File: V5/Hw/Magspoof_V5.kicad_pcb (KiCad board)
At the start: 2 copper layers, 76.5 x 32.5 mm, 59 parts, among them J1 SWD, J2 SWD, P1 USB_C_Plug_USB2.0, Q1 DMG3415U-7, SW1 ON, SW3 S1, SW4 SOURCE MAG, SW5 RESET, U1 CH552G, U2 AP2112K-3.3, U3 TC4424, U5 MCP73831

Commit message: feat(hw): logos
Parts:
- moved kibuzzard-6435F3C4 4.80 mm to (145.2, 50.0)
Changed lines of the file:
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@@
 	(footprint "kibuzzard-6435F3C4"
 		(layer "F.Cu")
-		(at 140.42 50.31 90)
+		(at 145.21 50.01 90)
 		(descr "Generated with KiBuzzard")
 		(tags "kb_params=eyJBbGlnbm1lbnRDaG9pY2UiOiAiQ2VudGVyIiwgIkNhcExlZnRDaG9pY2UiOiAiWyIsICJDYXBSaWdodENob2ljZSI6ICJdIiwgIkZvbnRDb21ib0JveCI6ICJVYnVudHVNb25vLUIiLCAiSGVpZ2h0Q3RybCI6ICIuOCIsICJMYXllckNvbWJvQm94IjogIkYuU2lsa1MiLCAiTXVsdGlMaW5lVGV4dCI6ICJDT0lMIiwgIlBhZGRpbmdCb3R0b21DdHJsIjogIjUiLCAiUGFkZGluZ0xlZnRDdHJsIjogIjUiLCAiUGFkZGluZ1JpZ2h0Q3RybCI6ICI1IiwgIlBhZGRpbmdUb3BDdHJsIjogIjUiLCAiV2lkdGhDdHJsIjogIiJ9")
@@
 		(tags "Through hole pin header THT 1x04 2.54mm single row")
 		(property "Reference" "J2"
-			(at 0 -2.33 270)
+			(at 0 -2.33 -90)
 			(layer "F.SilkS")
 			(effects
@@
 		)
 		(property "Value" "SWD"
-			(at 0 9.95 270)
+			(at 0 9.95 -90)
 			(layer "F.Fab")
 			(effects
@@
 		)
 		(fp_text user "${REFERENCE}"
-			(at 0 3.81 360)
+			(at 0 3.81 0)
 			(layer "F.Fab")
 			(effects

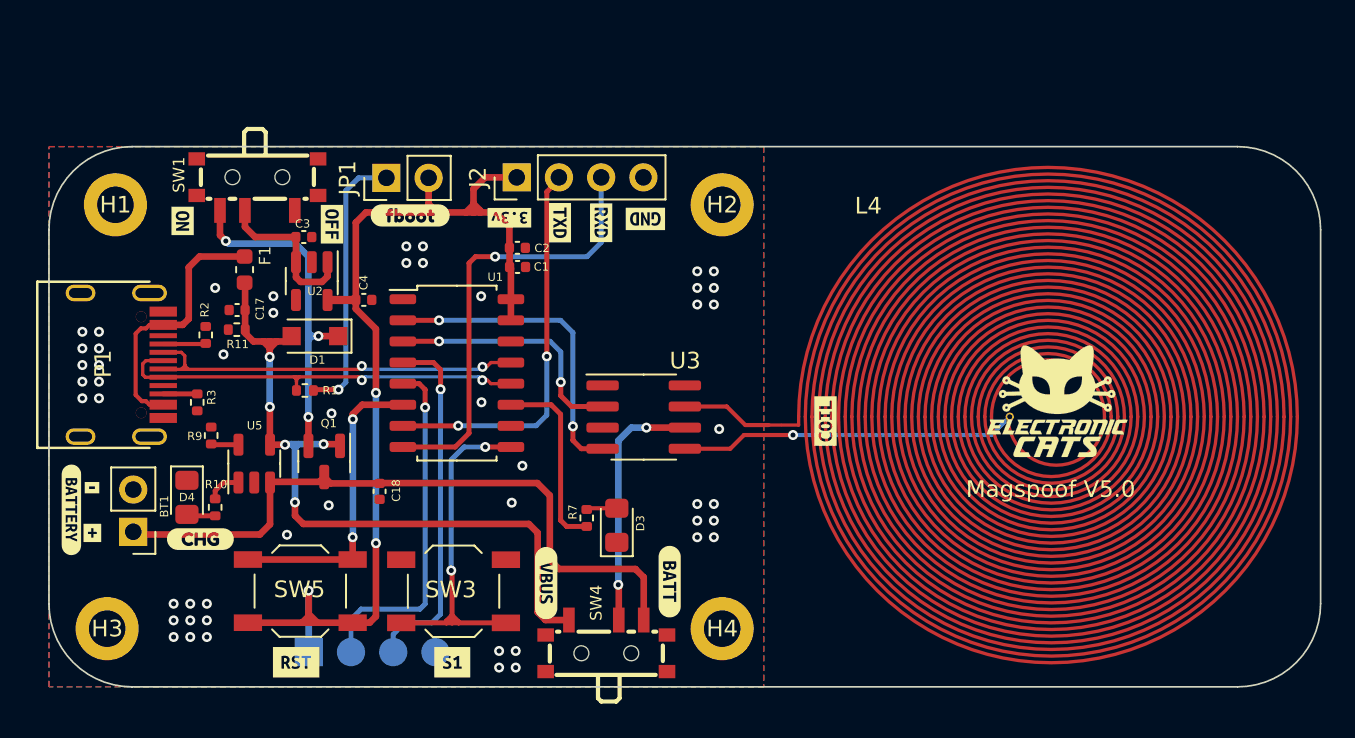
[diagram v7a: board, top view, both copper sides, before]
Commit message: feat(hw): components organization updated
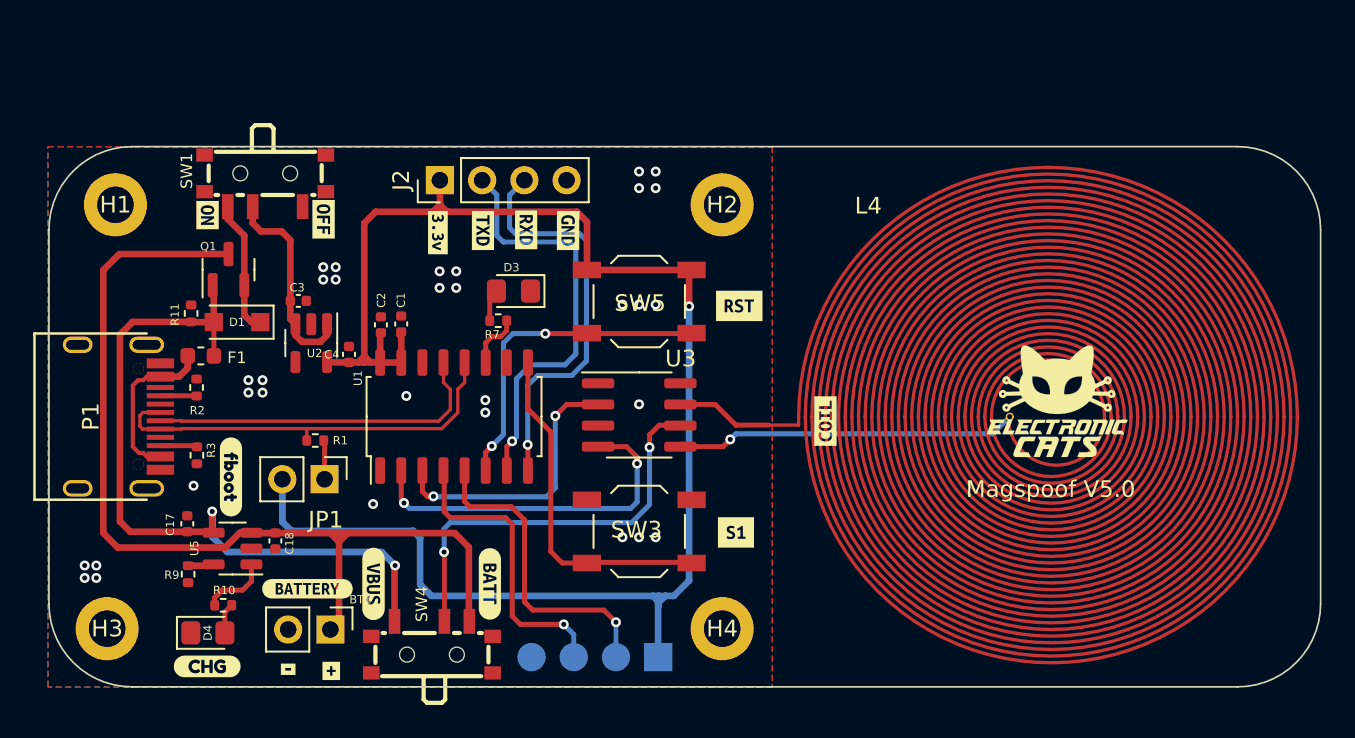
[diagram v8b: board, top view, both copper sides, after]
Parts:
- moved kibuzzard-660F1CC0 34.2 mm to (140.0, 43.1)
- moved SW5 26.8 mm to (134.0, 42.8), turned to 180 degrees
- moved kibuzzard-6616D983 22.1 mm to (135.2, 60.1)
- moved J1 21.0 mm to (135.2, 64.2), turned to 90 degrees
- moved kibuzzard-64665C9F 19.1 mm to (109.5, 53.4), turned to -90 degrees
- moved kibuzzard-660F1CCE 18.8 mm to (139.8, 56.7)
- moved JP1 18.5 mm to (115.1, 53.5), turned to -90 degrees
- moved kibuzzard-6436EA37 16.6 mm to (115.5, 65.0)
- moved kibuzzard-6616D9B1 16.2 mm to (132.6, 59.4)
- moved kibuzzard-6436EA46 16.1 mm to (112.9, 64.9)
- moved D3 15.4 mm to (126.4, 42.2), turned to 180 degrees
- moved kibuzzard-6616DCE6 15.0 mm to (114.0, 60.1), turned to 0 degrees
- moved BT1 13.2 mm to (115.4, 62.5), turned to -90 degrees
- moved C17 13.2 mm to (106.8, 56.2), turned to 90 degrees
- moved R7 13.0 mm to (125.5, 44.0), turned to 180 degrees
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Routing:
- net +3V3: track 65.8 -> 98.8 mm, vias 3 -> 1
- net +BATT: track 41.0 -> 58.9 mm
- net Net-(JP1-A): track 16.4 -> 2.35 mm, vias 1 -> 0
- net Net-(D1-K): track 21.2 -> 8.07 mm, vias 3 -> 0
- net Net-(SW4A-B): track 15.1 -> 24.8 mm
- net /LED: track 11.3 -> 3.35 mm
- net Net-(F1-Pad1): track 15.9 -> 10.1 mm
- net /RXD_BOOT: track 21.6 -> 17.9 mm
- net /D-: track 24.1 -> 20.7 mm, vias 2 -> 0
- net Net-(SW1-B): track 9.74 -> 13.0 mm
- net /IN_A: track 19.0 -> 21.6 mm
- net /TXD_BOOT: track 21.2 -> 19.0 mm
- net /RXD: track 26.9 -> 24.7 mm
- net /TXD: track 23.5 -> 25.8 mm, vias 2 -> 1
- net Net-(U5-STAT): track 2.09 -> 4.09 mm
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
